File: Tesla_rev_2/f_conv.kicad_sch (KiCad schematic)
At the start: 22 parts, among them J5 Conn_Coaxial, J6 Conn_Coaxial, U4 AD831, Y1 Crystal

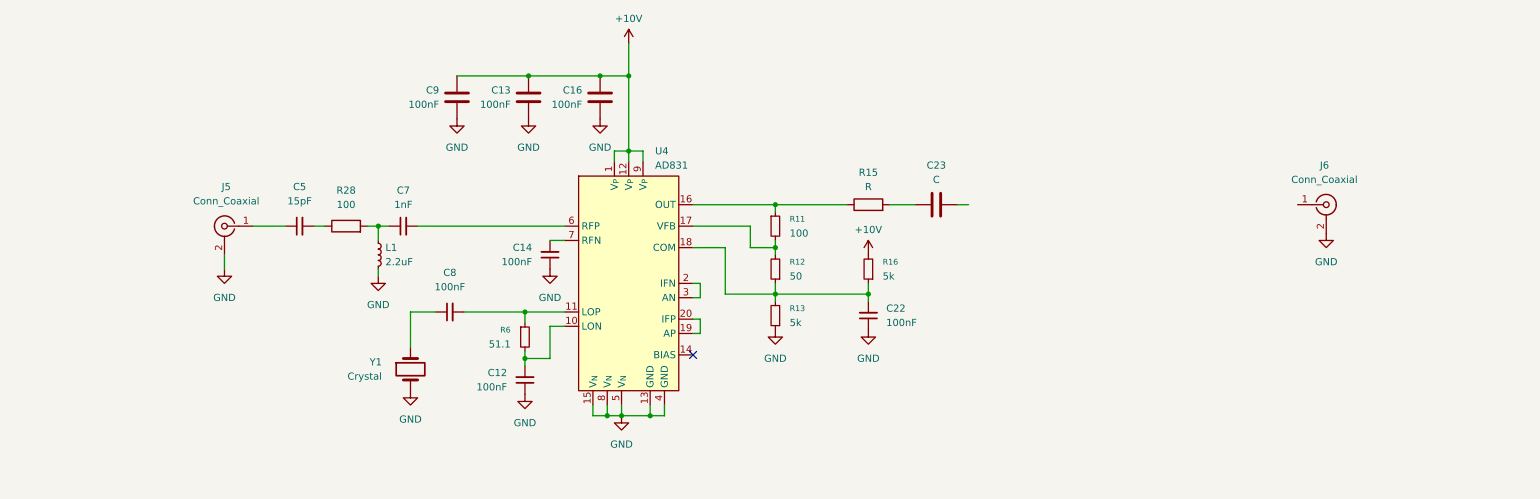
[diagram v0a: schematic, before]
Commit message: Rev 2.3, schematic and footprint fixes, prepared for layout
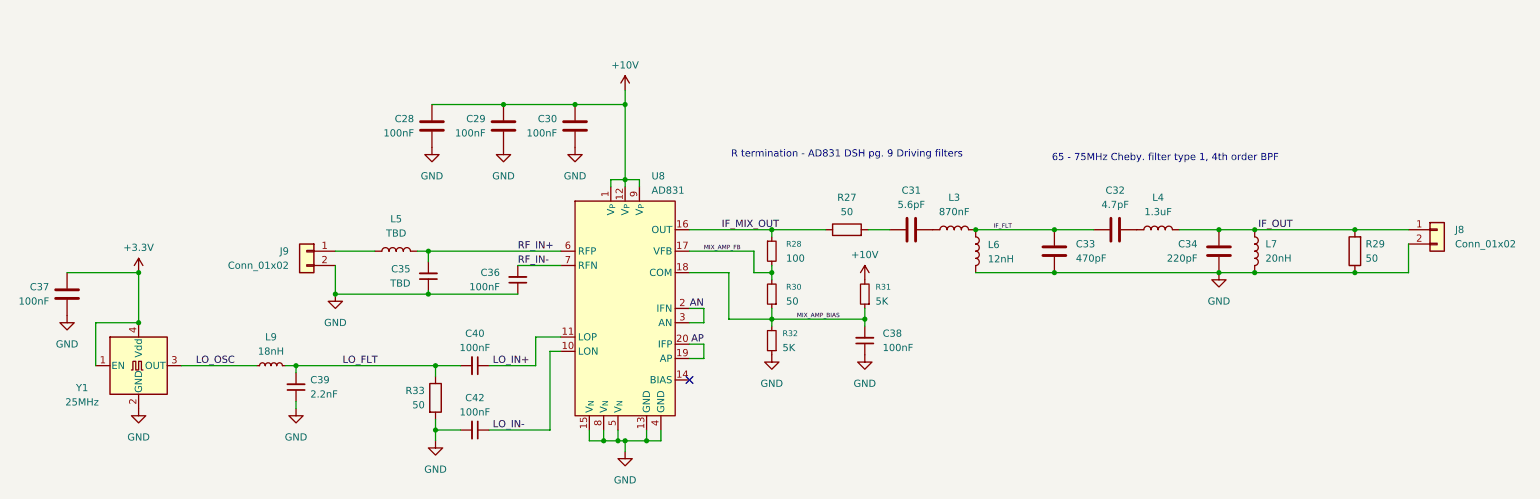
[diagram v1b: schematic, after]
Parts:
- removed C12, C8: 100nF, symbol Device:C_Small
- removed C23: C, symbol Device:C
- removed C5: 15pF, symbol Device:C_Small
- removed C7: 1nF, symbol Device:C_Small
- removed J5, J6: Conn_Coaxial, symbol Connector:Conn_Coaxial
- removed L1: 2.2uF, symbol Device:L_Small
- removed R28: 100, symbol Device:R
- removed R6: 51.1, symbol Device:R_Small
- removed Y1: Crystal, symbol Device:Crystal
- added C31: 5.6pF, Capacitor_SMD:C_0603_1608Metric, symbol Device:C
- added C32: 4.7pF, Capacitor_SMD:C_0603_1608Metric, symbol Device:C
- added C33: 470pF, Capacitor_SMD:C_0603_1608Metric, symbol Device:C
- added C34: 220pF, Capacitor_SMD:C_0603_1608Metric, symbol Device:C
- added C35: TBD, Capacitor_SMD:C_0805_2012Metric, symbol Device:C_Small
- added C37: 100nF, Capacitor_SMD:C_0805_2012Metric, symbol Device:C
- added C39: 2.2nF, Capacitor_SMD:C_0603_1608Metric, symbol Device:C_Small
- added C40, C42: 100nF, Capacitor_SMD:C_0805_2012Metric, symbol Device:C_Small
- added J8, J9: Conn_01x02, Tesla_Library:Conn_Solder_1x02_SMD, symbol Connector_Generic:Conn_01x02
- added L3: 870nF, Inductor_SMD:L_0805_2012Metric, symbol Device:L
- added L4: 1.3uF, Inductor_SMD:L_0805_2012Metric, symbol Device:L
- added L5: TBD, Inductor_SMD:L_0603_1608Metric, symbol Device:L
- added L6: 12nH, Inductor_SMD:L_0603_1608Metric, symbol Device:L
- added L7: 20nH, Inductor_SMD:L_0603_1608Metric, symbol Device:L
- added L9: 18nH, Inductor_SMD:L_0603_1608Metric, symbol Device:L_Small
- added R29, R33: 50, Capacitor_SMD:C_0805_2012Metric, symbol Device:R
- added Y1: 25MHz, Crystal:Crystal_SMD_0603-4Pin_6.0x3.5mm_HandSoldering, symbol Oscillator:ASE-xxxMHz
- C28: renamed from C9; footprint (none) -> Capacitor_SMD:C_0805_2012Metric
- C29: renamed from C13; footprint (none) -> Capacitor_SMD:C_0805_2012Metric
- C30: renamed from C16; footprint (none) -> Capacitor_SMD:C_0805_2012Metric
- C36: renamed from C14; footprint (none) -> Capacitor_SMD:C_0805_2012Metric
- C38: renamed from C22; footprint (none) -> Capacitor_SMD:C_0805_2012Metric
- R27: renamed from R15; value R -> 50; footprint (none) -> Capacitor_SMD:C_0805_2012Metric
- R28: renamed from R11; footprint (none) -> Capacitor_SMD:C_0805_2012Metric
- R30: renamed from R12; footprint (none) -> Capacitor_SMD:C_0805_2012Metric
- R31: renamed from R16; value 5k -> 5K; footprint (none) -> Capacitor_SMD:C_0805_2012Metric
- R32: renamed from R13; value 5k -> 5K; footprint (none) -> Capacitor_SMD:C_0805_2012Metric
- U8: renamed from U4; footprint (none) -> Package_LCC:PLCC-20
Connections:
- net GND: now also C33.1, C34.1, C35.1, C37.1, C39.1, C42.2, J8.2 (Pin_2), J9.2 (Pin_2), L6.1, L7.2, R29.1, R33.2, Y1.2 (GND)
- net IF_MIX_OUT: now reaches R27.1, R28.1, U8.16 (OUT)
- net MIX_AMP_FB: now reaches R28.2, R30.2, U8.17 (VFB)
- net MIX_AMP_BIAS: now reaches C38.2, R30.1, R31.1, R32.2, U8.18 (COM)
- net at R27.2: now also C31.1
- net LO_IN-: now reaches U8.10 (LON)
- net LO_IN-: now also C42.1
- net RF_IN-: now reaches C36.2, U8.7 (RFN)
- net RF_IN+: now reaches U8.6 (RFP)
- net RF_IN+: now also C35.2, L5.1
- net LO_IN+: now reaches U8.11 (LOP)
- net LO_IN+: now also C40.1
- net AP: now reaches U8.19 (AP), U8.20 (IFP)
- net AN: now reaches U8.2 (IFN), U8.3 (AN)
- new net: J9.1 (Pin_1), L5.2
- new net: C31.2, L3.2
- new net: C32.1, L4.2
- new net +3.3V: C37.2, Y1.1 (EN), Y1.4 (Vdd)
- new net IF_FLT: C32.2, C33.2, L3.1, L6.2
- new net IF_OUT: C34.2, J8.1 (Pin_1), L4.1, L7.1, R29.2
- new net LO_FLT: C39.2, C40.2, L9.2, R33.1
- new net LO_OSC: L9.1, Y1.3 (OUT)
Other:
- note added: "65 - 75MHz Cheby. filter type 1, 4th order BPF"
- note added: "R termination - AD831 DSH pg. 9 Driving filters"
- title: Tesla sextant BT -> Frequency converter
- moved on the sheet: C28, C29, C30, C36, C38, R27, R28, R30, R31, R32, U8

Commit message: added PCB layou
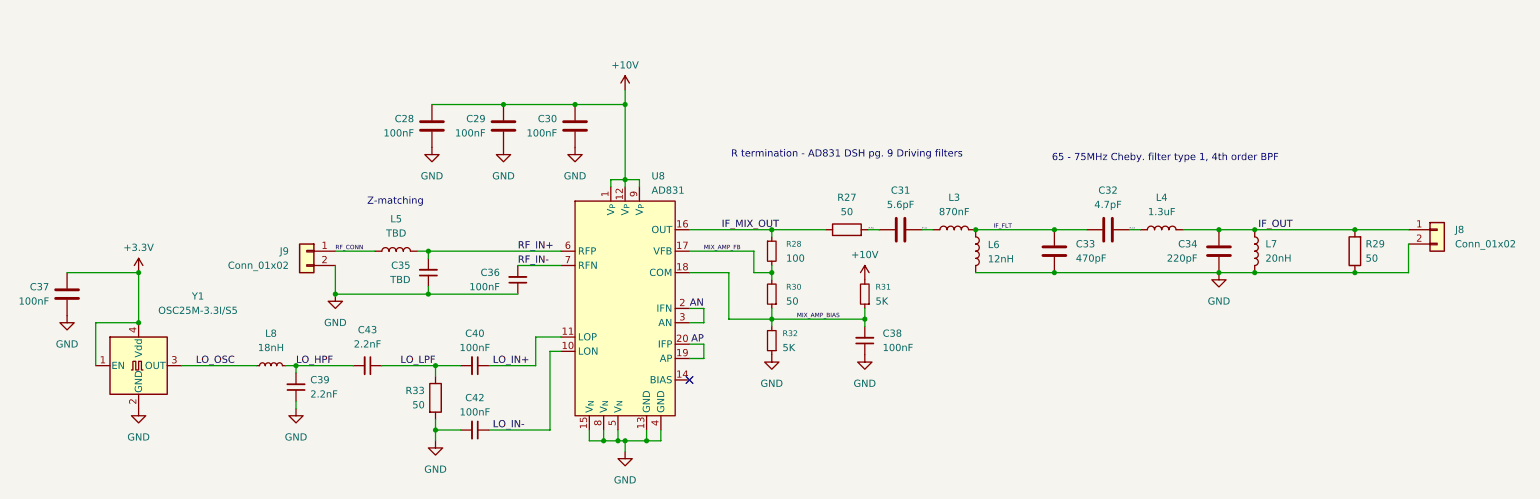
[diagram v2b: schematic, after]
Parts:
- added C43: 2.2nF, Capacitor_SMD:C_0603_1608Metric, symbol Device:C_Small
- C40, C42: footprint Capacitor_SMD:C_0805_2012Metric -> Capacitor_SMD:C_0603_1608Metric
- Y1: value 25MHz -> OSC25M-3.3I/S5; footprint Crystal:Crystal_SMD_0603-4Pin_6.0x3.5mm_HandSoldering -> Oscillator:Oscillator_SMD_Fordahl_DFAS15-4Pin_5.0x3.2mm_HandSoldering
- renumbered L9 to L8
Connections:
- net RF_CONN: now reaches J9.1 (Pin_1), L5.2
- net IF_R1: now reaches C31.1, R27.2
- net IF_C1: now reaches C31.2, L3.2
- net IF_C3: now reaches C32.1, L4.2
- net LO_FLT renamed LO_HPF
- net LO_HPF: now also C43.2; no longer C40.2, R33.1
- new net LO_LPF: C40.2, C43.1, R33.1
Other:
- note added: "Z-matching"
- moved on the sheet: C31, C32, C35, L4
